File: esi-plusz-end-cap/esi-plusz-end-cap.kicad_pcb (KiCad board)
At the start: 4 copper layers, 105.6 x 105.6 mm, 55 parts, among them J1 M55-7011242R, J2 U.FL-R-SMA, U1 RM3100, U2 RM3100

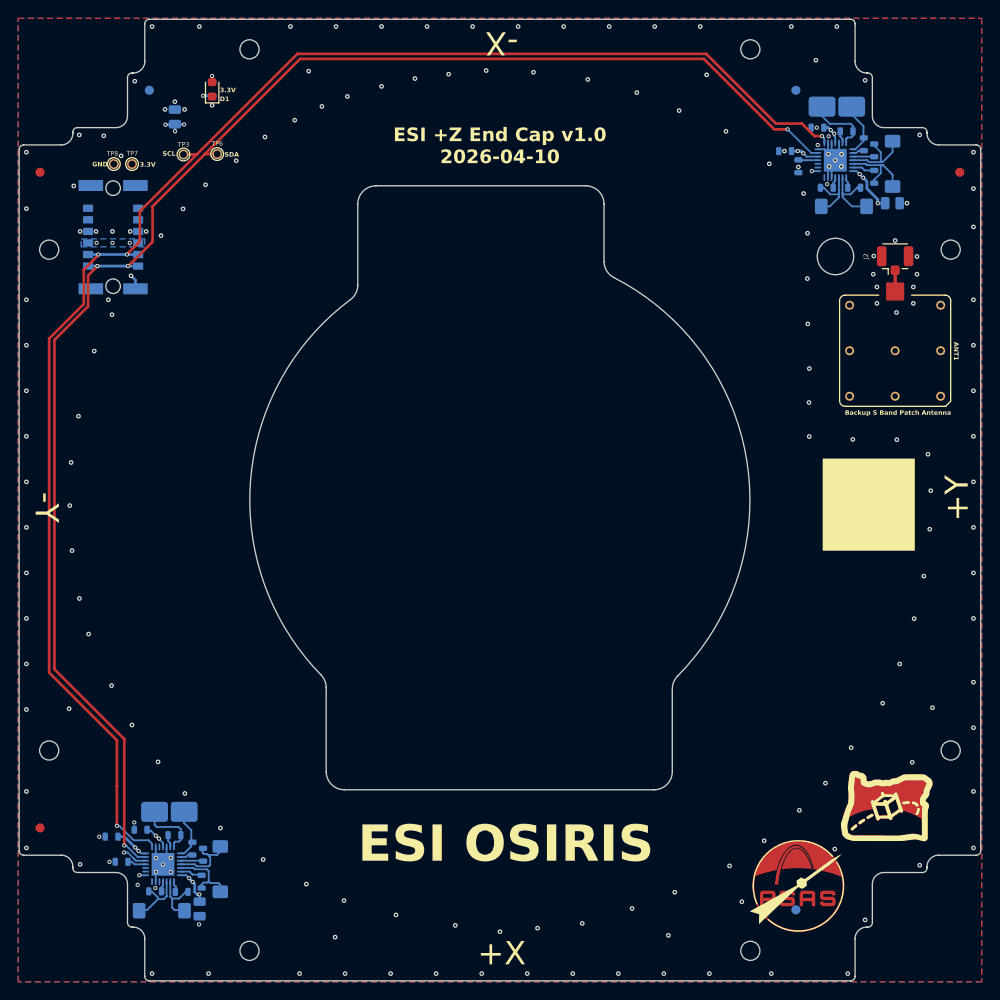
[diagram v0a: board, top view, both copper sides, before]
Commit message: New ESI dxf w/ square cutout
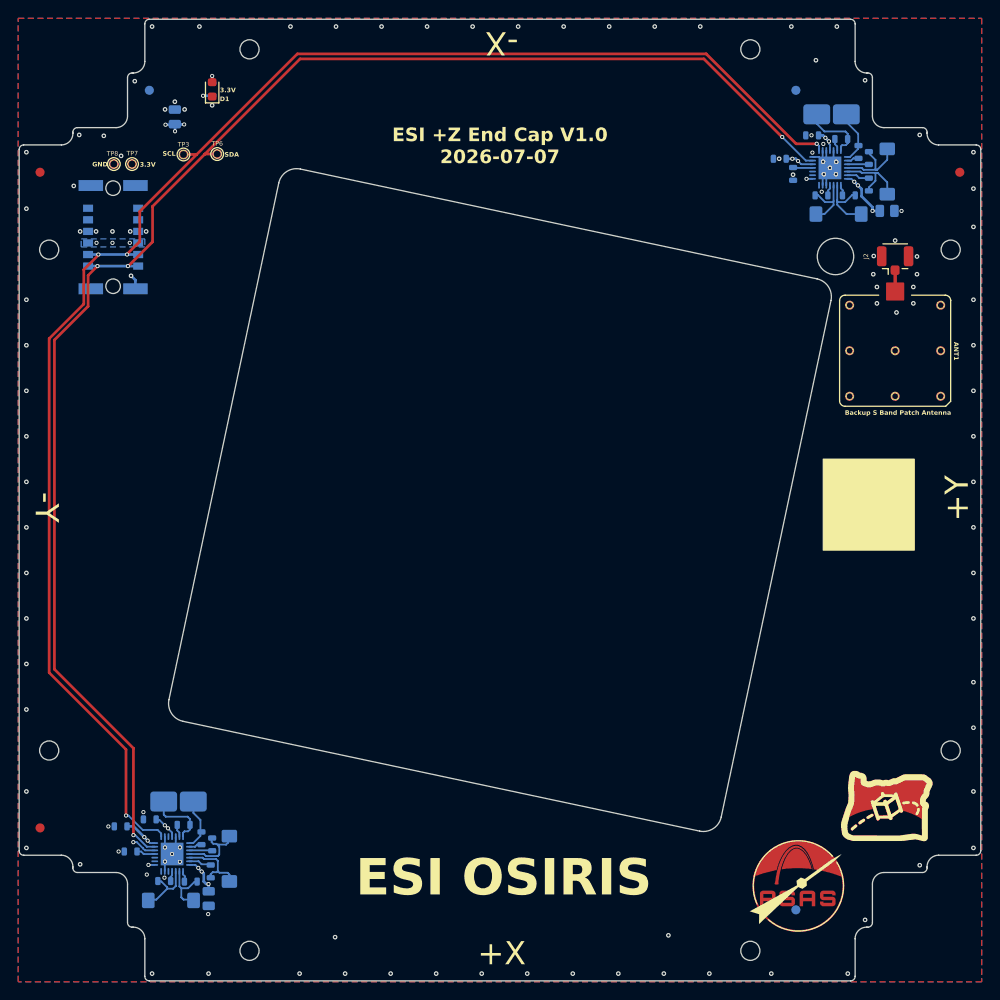
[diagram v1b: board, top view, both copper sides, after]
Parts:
- moved C3 1.51 mm to (116.5, 148.8)
- moved L9 1.51 mm to (113.2, 138.1)
- moved R14 1.51 mm to (113.8, 140.7)
- moved C5 1.51 mm to (106.9, 140.8)
- moved C7 1.51 mm to (110.0, 140.1)
- moved L7 1.51 mm to (112.4, 149.0)
- moved L8 1.51 mm to (118.8, 144.4)
- moved R10 1.51 mm to (114.5, 146.9)
- moved R11 1.51 mm to (111.6, 146.8)
- moved R12 1.51 mm to (116.9, 142.8)
- moved R13 1.51 mm to (116.7, 145.8)
- moved R15 1.51 mm to (115.7, 142.1)
- moved R9 1.51 mm to (108.0, 143.6)
- moved U1 1.51 mm to (112.5, 143.9)
- moved C2 1.03 mm to (191.0, 73.2)
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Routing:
- net /MAG-SDA: track 170.4 -> 169.4 mm
- net /MAG-SCL: track 172.0 -> 171.1 mm
- net GND: vias 183 -> 113
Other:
- outline, holes or cut-outs redrawn
- board text added: "ESI +Z End Cap V1.0 2026-07-07"
- board text removed: "${TITLE} v${REVISION} ${ISSUE_DATE}"
